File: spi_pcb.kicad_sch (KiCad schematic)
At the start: 15 parts, among them J1 GPIO, J2 PWR, U1 LMZ23605TZ

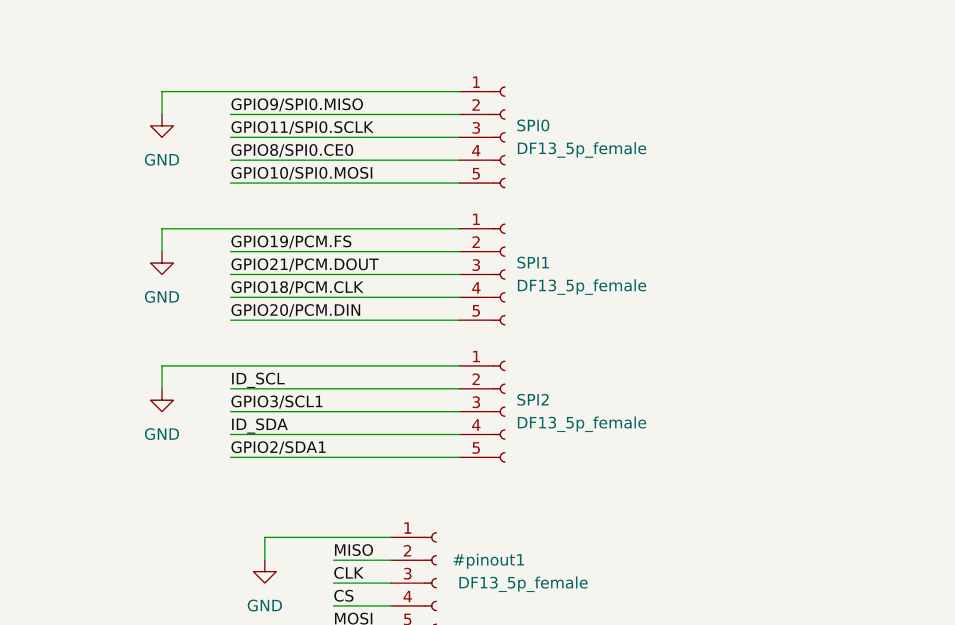
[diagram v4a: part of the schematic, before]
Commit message: Rerouted for 0.25mm copper clearance. Added sample SPI impedance matching resistor.
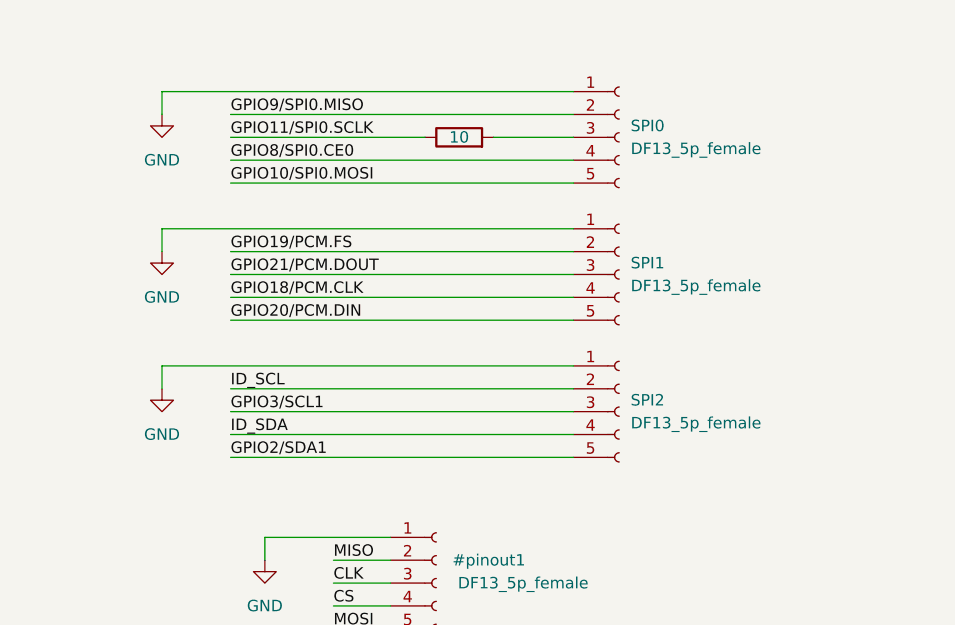
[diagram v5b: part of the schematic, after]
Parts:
- added R3: 10, Resistor_SMD:R_0402_1005Metric_Pad0.72x0.64mm_HandSolder, symbol Device:R
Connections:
- net GPIO11/SPI0.SCLK: now also R3.1; no longer SPI0.3 (Pin_3)
- new net: R3.2, SPI0.3 (Pin_3)
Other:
- moved on the sheet: SPI0, SPI1, SPI2
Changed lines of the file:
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@@
 	(wire
 		(pts
-			(xy 127 67.31) (xy 152.4 67.31)
+			(xy 127 67.31) (xy 165.1 67.31)
 		)
 		(stroke
@@
 	(wire
 		(pts
-			(xy 127 36.83) (xy 152.4 36.83)
+			(xy 127 36.83) (xy 165.1 36.83)
 		)
 		(stroke
@@
 	(wire
 		(pts
-			(xy 119.38 57.15) (xy 152.4 57.15)
+			(xy 119.38 57.15) (xy 165.1 57.15)
 		)
 		(stroke
@@
 	(wire
 		(pts
-			(xy 127 34.29) (xy 152.4 34.29)
+			(xy 127 34.29) (xy 165.1 34.29)
 		)
 		(stroke
@@
 	(wire
 		(pts
-			(xy 127 64.77) (xy 152.4 64.77)
+			(xy 127 64.77) (xy 165.1 64.77)
 		)
 		(stroke
@@
 	(wire
 		(pts
-			(xy 127 62.23) (xy 152.4 62.23)
+			(xy 127 62.23) (xy 165.1 62.23)
 		)
 		(stroke
@@
 	(wire
 		(pts
-			(xy 127 52.07) (xy 152.4 52.07)
+			(xy 127 52.07) (xy 165.1 52.07)
 		)
 		(stroke
@@
 	(wire
 		(pts
-			(xy 127 31.75) (xy 152.4 31.75)
+			(xy 127 31.75) (xy 148.59 31.75)
 		)
 		(stroke
@@
 	(wire
 		(pts
-			(xy 127 59.69) (xy 152.4 59.69)
+			(xy 127 59.69) (xy 165.1 59.69)
 		)
 		(stroke
@@
 	(wire
 		(pts
-			(xy 127 29.21) (xy 152.4 29.21)
+			(xy 127 29.21) (xy 165.1 29.21)
 		)
 		(stroke
@@
 	(wire
 		(pts
-			(xy 127 49.53) (xy 152.4 49.53)
+			(xy 127 49.53) (xy 165.1 49.53)
 		)
 		(stroke
@@
 	(wire
 		(pts
-			(xy 119.38 41.91) (xy 152.4 41.91)
+			(xy 119.38 41.91) (xy 165.1 41.91)
 		)
 		(stroke
@@
 	(wire
 		(pts
-			(xy 127 44.45) (xy 152.4 44.45)
+			(xy 127 44.45) (xy 165.1 44.45)
 		)
 		(stroke
@@
 	(wire
 		(pts
-			(xy 119.38 26.67) (xy 152.4 26.67)
+			(xy 119.38 26.67) (xy 165.1 26.67)
 		)
 		(stroke
@@
 	(wire
 		(pts
+			(xy 165.1 31.75) (xy 156.21 31.75)
+		)
+		(stroke
+			(width 0)
+			(type default)
+		)
+	)
+	(wire
+		(pts
 			(xy 119.38 96.52) (xy 119.38 99.06)
 		)
@@
 	(wire
 		(pts
-			(xy 127 46.99) (xy 152.4 46.99)
+			(xy 127 46.99) (xy 165.1 46.99)
 		)
 		(stroke
@@
 	(symbol
 		(lib_id "Connector:Conn_01x05_Socket")
-		(at 157.48 31.75 0)
+		(at 170.18 31.75 0)
 		(unit 1)
 		(exclude_from_sim no)
@@
 		(dnp no)
 		(property "Reference" "SPI0"
-			(at 158.75 30.4799 0)
+			(at 171.45 30.4799 0)
 			(effects
 				(font
@@
 		)
 		(property "Value" "DF13_5p_female"
-			(at 158.75 33.0199 0)
+			(at 171.45 33.0199 0)
 			(effects
 				(font
@@
 		)
 		(property "Footprint" "Connector_Hirose:Hirose_DF13-05P-1.25DS_1x05_P1.25mm_Horizontal"
-			(at 157.48 31.75 0)
+			(at 170.18 31.75 0)
 			(effects
 				(font
@@
 		)
 		(property "Datasheet" "~"
-			(at 157.48 31.75 0)
+			(at 170.18 31.75 0)
 			(effects
 				(font
@@
 		)
 		(property "Description" "Generic connector, single row, 01x05, script generated"
-			(at 157.48 31.75 0)
+			(at 170.18 31.75 0)
 			(effects
 				(font
@@
 	(symbol
 		(lib_id "Connector:Conn_01x05_Socket")
-		(at 157.48 46.99 0)
+		(at 170.18 46.99 0)
 		(unit 1)
 		(exclude_from_sim no)
@@
 		(dnp no)
 		(property "Reference" "SPI1"
-			(at 158.75 45.7199 0)
+			(at 171.45 45.7199 0)
 			(effects
 				(font
@@
 		)
 		(property "Value" "DF13_5p_female"
-			(at 158.75 48.2599 0)
+			(at 171.45 48.2599 0)
 			(effects
 				(font
@@
 		)
 		(property "Footprint" "Connector_Hirose:Hirose_DF13-05P-1.25DS_1x05_P1.25mm_Horizontal"
-			(at 157.48 46.99 0)
+			(at 170.18 46.99 0)
 			(effects
 				(font
@@
 		)
 		(property "Datasheet" "~"
-			(at 157.48 46.99 0)
+			(at 170.18 46.99 0)
 			(effects
 				(font
@@
 		)
 		(property "Description" "Generic connector, single row, 01x05, script generated"
-			(at 157.48 46.99 0)
+			(at 170.18 46.99 0)
 			(effects
 				(font
@@
 	)
 	(symbol
+		(lib_id "Device:R")
+		(at 152.4 31.75 90)
+		(unit 1)
+		(exclude_from_sim no)
+		(in_bom yes)
+		(on_board yes)
+		(dnp no)
+		(property "Reference" "R3"
+			(at 152.4 25.4 90)
+			(effects
+				(font
+					(size 1.27 1.27)
+				)
+				(hide yes)
+			)
+		)
+		(property "Value" "10"
+			(at 152.4 31.75 90)
+			(effects
+				(font
+					(size 1.27 1.27)
+				)
+			)
+		)
+		(property "Footprint" "Resistor_SMD:R_0402_1005Metric_Pad0.72x0.64mm_HandSolder"
+			(at 152.4 33.528 90)
+			(effects
+				(font
+					(size 1.27 1.27)
+				)
+				(hide yes)
+			)
+		)
+		(property "Datasheet" "~"
+			(at 152.4 31.75 0)
+			(effects
+				(font
+					(size 1.27 1.27)
+				)
+				(hide yes)
+			)
+		)
+		(property "Description" "Resistor"
+			(at 152.4 31.75 0)
+			(effects
+				(font
+					(size 1.27 1.27)
+				)
+				(hide yes)
+			)
+		)
+		(pin "2"
+		)
+		(pin "1"
+		)
+		(instances
+			(project ""
+				(path "/e63e39d7-6ac0-4ffd-8aa3-1841a4541b55"
+					(reference "R3")
+					(unit 1)
+				)
+			)
+		)
+	)
+	(symbol
 		(lib_id "Connector:Conn_01x05_Socket")
-		(at 157.48 62.23 0)
+		(at 170.18 62.23 0)
 		(unit 1)
 		(exclude_from_sim no)
@@
 		(dnp no)
 		(property "Reference" "SPI2"
-			(at 158.75 60.9599 0)
+			(at 171.45 60.9599 0)
 			(effects
 				(font
@@
 		)
 		(property "Value" "DF13_5p_female"
-			(at 158.75 63.4999 0)
+			(at 171.45 63.4999 0)
 			(effects
 				(font
@@
 		)
 		(property "Footprint" "Connector_Hirose:Hirose_DF13-05P-1.25DS_1x05_P1.25mm_Horizontal"
-			(at 157.48 62.23 0)
+			(at 170.18 62.23 0)
 			(effects
 				(font
@@
 		)
 		(property "Datasheet" "~"
-			(at 157.48 62.23 0)
+			(at 170.18 62.23 0)
 			(effects
 				(font
@@
 		)
 		(property "Description" "Generic connector, single row, 01x05, script generated"
-			(at 157.48 62.23 0)
+			(at 170.18 62.23 0)
 			(effects
 				(font

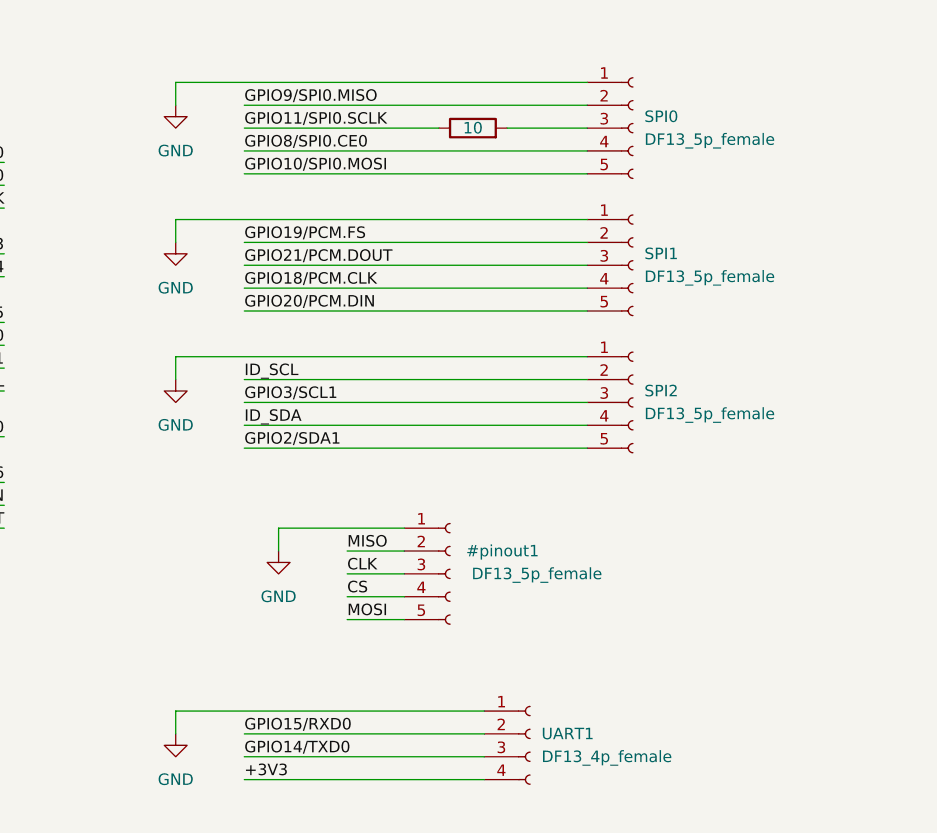
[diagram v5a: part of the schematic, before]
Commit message: Cut cooling hole for Raspberry CPU, redone vias. Added 10 Ohm impedance matching for source SPI signals.
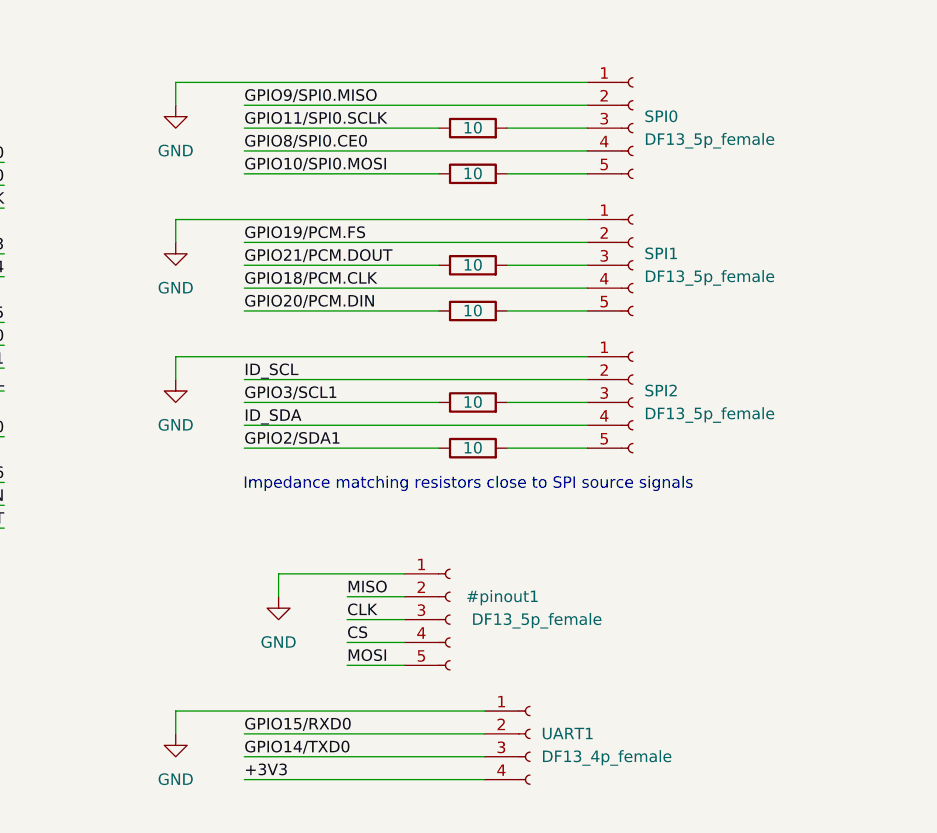
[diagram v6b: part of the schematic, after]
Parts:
- added R4, R5, R6, R7, R8: 10, Resistor_SMD:R_0402_1005Metric_Pad0.72x0.64mm_HandSolder, symbol Device:R
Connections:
- net GPIO10/SPI0.MOSI: now also R4.1; no longer SPI0.5 (Pin_5)
- net GPIO20/PCM.DIN: now also R5.1; no longer SPI1.5 (Pin_5)
- net GPIO21/PCM.DOUT: now also R6.1; no longer SPI1.3 (Pin_3)
- net GPIO2/SDA1: now also R8.1; no longer SPI2.5 (Pin_5)
- net GPIO3/SCL1: now also R7.1; no longer SPI2.3 (Pin_3)
- new net: R6.2, SPI1.3 (Pin_3)
- new net: R4.2, SPI0.5 (Pin_5)
- new net: R5.2, SPI1.5 (Pin_5)
- new net: R7.2, SPI2.3 (Pin_3)
- new net: R8.2, SPI2.5 (Pin_5)
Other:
- note added: "Impedance matching resistors close to SPI source signals"

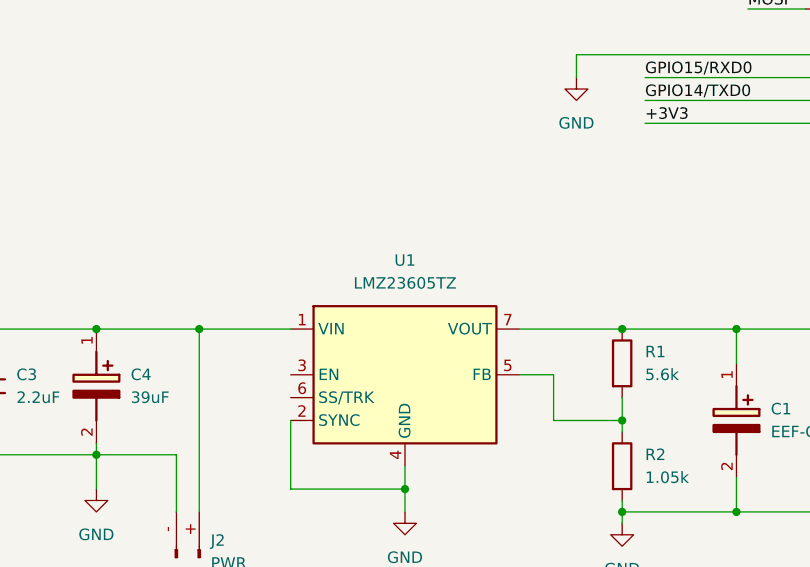
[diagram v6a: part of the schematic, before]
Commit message: Move power connector a bit closer to centre. Add project library.
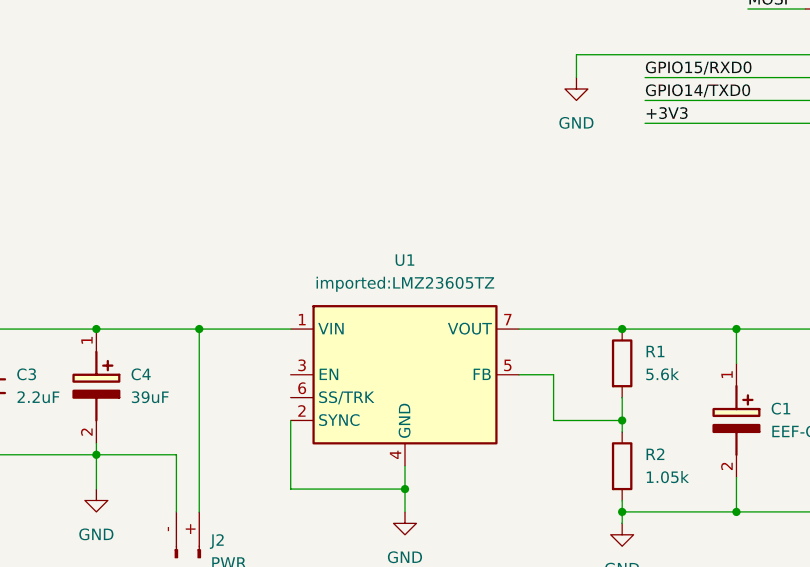
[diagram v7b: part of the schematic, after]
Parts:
- C1: footprint EEFCX0J101R -> imported:EEFCX0J101R
- C2: footprint CAPC3216X180N -> imported:CAPC3216X180N
- C3, C5: footprint CAPC1608X90N -> imported:CAPC1608X90N
- C4: footprint 16SVPT560M -> imported:16SVPT560M
- U1: value LMZ23605TZ -> imported:LMZ23605TZ
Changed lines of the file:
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@@
 			)
 		)
-		(property "Footprint" "16SVPT560M"
+		(property "Footprint" "imported:16SVPT560M"
 			(at -30.15 135.89 0)
 			(effects
@@
 			)
 		)
-		(property "Value" "LMZ23605TZ"
+		(property "Value" "imported:LMZ23605TZ"
 			(at 100.33 121.92 0)
 			(effects
@@
 			)
 		)
-		(property "Footprint" "EEFCX0J101R"
+		(property "Footprint" "imported:EEFCX0J101R"
 			(at 40.97 139.7 0)
 			(effects
@@
 			)
 		)
-		(property "Footprint" "CAPC1608X90N"
+		(property "Footprint" "imported:CAPC1608X90N"
 			(at -55.55 135.89 0)
 			(effects
@@
 			)
 		)
-		(property "Footprint" "CAPC1608X90N"
+		(property "Footprint" "imported:CAPC1608X90N"
 			(at -42.85 135.89 0)
 			(effects
@@
 			)
 		)
-		(property "Footprint" "CAPC3216X180N"
+		(property "Footprint" "imported:CAPC3216X180N"
 			(at 65.1 139.7 0)
 			(effects

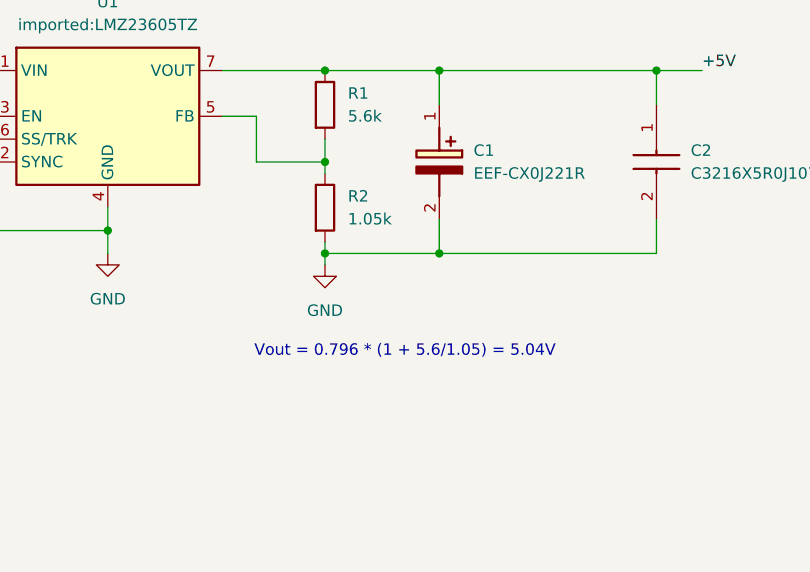
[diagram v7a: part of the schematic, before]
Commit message: Split feedback resistors into available values.
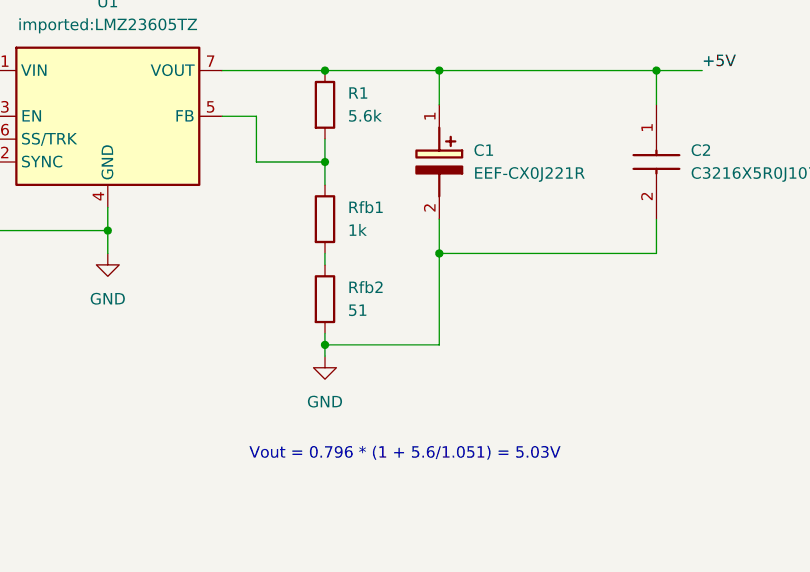
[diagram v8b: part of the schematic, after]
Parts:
- added Rfb1: 1k, Resistor_SMD:R_0603_1608Metric, symbol Device:R
- Rfb2: renamed from R2; value 1.05k -> 51
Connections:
- net at R1.2, U1.5 (FB): now also Rfb1.1; no longer Rfb2.1
- new net: Rfb1.2, Rfb2.1
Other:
- note added: "Vout = 0.796 * (1 + 5.6/1.051) = 5.03V"
- note removed: "Vout = 0.796 * (1 + 5.6/1.05) = 5.04V"
- moved on the sheet: Rfb2
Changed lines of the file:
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@@
 		)
 	)
-	(text "Vout = 0.796 * (1 + 5.6/1.05) = 5.04V"
+	(text "Vout = 0.796 * (1 + 5.6/1.051) = 5.03V"
 		(exclude_from_sim no)
-		(at 133.35 158.242 0)
+		(at 133.35 169.672 0)
 		(effects
 			(font
@@
 	)
 	(junction
+		(at 137.16 147.32)
+		(diameter 0)
+		(color 0 0 0 0)
+	)
+	(junction
 		(at 76.2 43.18)
 		(diameter 1.016)
@@
 	)
 	(junction
-		(at 137.16 147.32)
-		(diameter 0)
-		(color 0 0 0 0)
-	)
-	(junction
 		(at 76.2 68.58)
 		(diameter 1.016)
@@
 	)
 	(junction
-		(at 124.46 147.32)
-		(diameter 0)
-		(color 0 0 0 0)
-	)
-	(junction
 		(at 76.2 63.5)
 		(diameter 1.016)
@@
 	)
 	(junction
+		(at 124.46 157.48)
+		(diameter 0)
+		(color 0 0 0 0)
+	)
+	(junction
 		(at 55.88 27.94)
 		(diameter 1.016)
@@
 	(wire
 		(pts
-			(xy 124.46 137.16) (xy 124.46 138.43)
+			(xy 124.46 137.16) (xy 124.46 139.7)
 		)
 		(stroke
@@
 	(wire
 		(pts
+			(xy 137.16 147.32) (xy 137.16 157.48)
+		)
+		(stroke
+			(width 0)
+			(type default)
+		)
+	)
+	(wire
+		(pts
 			(xy 113.03 127) (xy 124.46 127)
 		)
@@
 	(wire
 		(pts
-			(xy 124.46 146.05) (xy 124.46 147.32)
+			(xy 124.46 156.21) (xy 124.46 157.48)
 		)
 		(stroke
@@
 	(wire
 		(pts
+			(xy 137.16 157.48) (xy 124.46 157.48)
+		)
+		(stroke
+			(width 0)
+			(type default)
+		)
+	)
+	(wire
+		(pts
 			(xy 31.75 45.72) (xy 60.96 45.72)
 		)
@@
 	(wire
 		(pts
-			(xy 124.46 147.32) (xy 137.16 147.32)
-		)
-		(stroke
-			(width 0)
-			(type default)
-		)
-	)
-	(wire
-		(pts
 			(xy 73.66 66.04) (xy 100.33 66.04)
 		)
@@
 	(wire
 		(pts
-			(xy 124.46 147.32) (xy 124.46 148.59)
+			(xy 76.2 68.58) (xy 76.2 80.01)
 		)
 		(stroke
 			(width 0)
-			(type default)
+			(type solid)
 		)
 	)
 	(wire
 		(pts
-			(xy 76.2 68.58) (xy 76.2 80.01)
+			(xy 73.66 53.34) (xy 100.33 53.34)
 		)
 		(stroke
@@
 	(wire
 		(pts
-			(xy 73.66 53.34) (xy 100.33 53.34)
+			(xy 60.96 68.58) (xy 31.75 68.58)
 		)
 		(stroke
@@
 	(wire
 		(pts
-			(xy 60.96 68.58) (xy 31.75 68.58)
+			(xy 77.47 127) (xy 87.63 127)
 		)
 		(stroke
 			(width 0)
-			(type solid)
+			(type default)
 		)
 	)
 	(wire
 		(pts
-			(xy 77.47 127) (xy 87.63 127)
+			(xy 124.46 157.48) (xy 124.46 158.75)
 		)
 		(stroke
@@
 	(wire
 		(pts
+			(xy 124.46 147.32) (xy 124.46 148.59)
+		)
+		(stroke
+			(width 0)
+			(type default)
+		)
+	)
+	(wire
+		(pts
 			(xy 156.21 46.99) (xy 165.1 46.99)
 		)
@@
 	(symbol
 		(lib_id "Device:R")
-		(at 124.46 142.24 0)
+		(at 124.46 152.4 0)
 		(unit 1)
 		(exclude_from_sim no)
@@
 		(dnp no)
 		(fields_autoplaced yes)
-		(property "Reference" "R2"
-			(at 127 140.9699 0)
+		(property "Reference" "Rfb2"
+			(at 127 151.1299 0)
 			(effects
 				(font
@@
 			)
 		)
-		(property "Value" "1.05k"
-			(at 127 143.5099 0)
+		(property "Value" "51"
+			(at 127 153.6699 0)
 			(effects
 				(font
@@
 		)
 		(property "Footprint" "Resistor_SMD:R_0603_1608Metric"
-			(at 122.682 142.24 90)
+			(at 122.682 152.4 90)
 			(effects
 				(font
@@
 		)
 		(property "Datasheet" "https://fr.farnell.com/multicomp-pro/mcwr06x1051ftl/resist-1k05-1-0-1w-couche-epaisse/dp/2447273"
-			(at 124.46 142.24 0)
+			(at 124.46 152.4 0)
 			(effects
 				(font
@@
 		)
 		(property "Description" "Resistor"
-			(at 124.46 142.24 0)
+			(at 124.46 152.4 0)
 			(effects
 				(font
@@
 			(project ""
 				(path "/e63e39d7-6ac0-4ffd-8aa3-1841a4541b55"
-					(reference "R2")
+					(reference "Rfb2")
 					(unit 1)
 				)
@@
 	(symbol
 		(lib_id "power:GND")
-		(at 124.46 148.59 0)
+		(at 124.46 158.75 0)
 		(unit 1)
 		(exclude_from_sim no)
@@
 		(fields_autoplaced yes)
 		(property "Reference" "#PWR012"
-			(at 124.46 154.94 0)
+			(at 124.46 165.1 0)
 			(effects
 				(font
@@
 		)
 		(property "Value" "GND"
-			(at 124.46 153.67 0)
+			(at 124.46 163.83 0)
 			(effects
 				(font
@@
 		)
 		(property "Footprint" ""
-			(at 124.46 148.59 0)
+			(at 124.46 158.75 0)
 			(effects
 				(font
@@
 		)
 		(property "Datasheet" ""
-			(at 124.46 148.59 0)
+			(at 124.46 158.75 0)
 			(effects
 				(font
@@
 		)
 		(property "Description" "Power symbol creates a global label with name \"GND\" , ground"
-			(at 124.46 148.59 0)
+			(at 124.46 158.75 0)
 			(effects
 				(font
@@
 					(unit 1)
 				)
+			)
+		)
+	)
+	(symbol
+		(lib_id "Device:R")
+		(at 124.46 143.51 0)
+		(unit 1)
+		(exclude_from_sim no)
+		(in_bom yes)
+		(on_board yes)
+		(dnp no)
+		(fields_autoplaced yes)
+		(property "Reference" "Rfb1"
+			(at 127 142.2399 0)
+			(effects
+				(font
+					(size 1.27 1.27)
+				)
+				(justify left)
+			)
+		)
+		(property "Value" "1k"
+			(at 127 144.7799 0)
+			(effects
+				(font
+					(size 1.27 1.27)
+				)
+				(justify left)
+			)
+		)
+		(property "Footprint" "Resistor_SMD:R_0603_1608Metric"
+			(at 122.682 143.51 90)
+			(effects
+				(font
+					(size 1.27 1.27)
+				)
+				(hide yes)
+			)
+		)
+		(property "Datasheet" "https://fr.farnell.com/multicomp-pro/mcwr06x1051ftl/resist-1k05-1-0-1w-couche-epaisse/dp/2447273"
+			(at 124.46 143.51 0)
+			(effects
+				(font
+					(size 1.27 1.27)
+				)
+				(hide yes)
+			)
+		)
+		(property "Description" "Resistor"
+			(at 124.46 143.51 0)
+			(effects
+				(font
+					(size 1.27 1.27)
+				)
+				(hide yes)
+			)
+		)
+		(pin "2"
+		)
+		(pin "1"
+		)
+		(instances
+			(project "spi_pcb"
+				(path "/e63e39d7-6ac0-4ffd-8aa3-1841a4541b55"
+					(reference "Rfb1")
+					(unit 1)
+				)
